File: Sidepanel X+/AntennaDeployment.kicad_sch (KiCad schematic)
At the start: 5 parts, among them Q1 BSS214NW

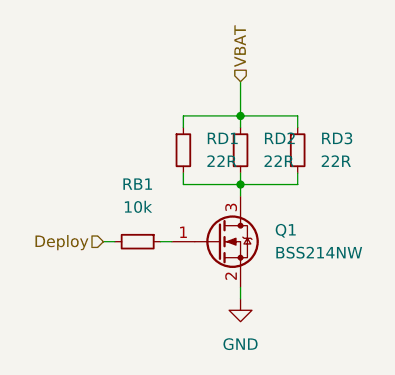
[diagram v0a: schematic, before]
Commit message: Changed the layout of all the sidepanel PCBs to mitigate the problems that arised from the bad previous design.
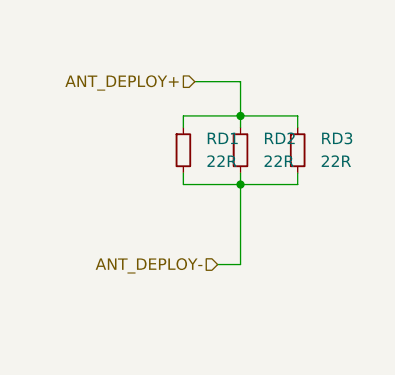
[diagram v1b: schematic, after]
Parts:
- removed Q1: BSS214NW, Package_TO_SOT_SMD:SOT-323_SC-70, symbol Transistor_FET:BSS214NW
- removed RB1: 10k, Resistor_SMD:R_0603_1608Metric, symbol Device:R_Small
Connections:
- net ANT_DEPLOY-: now reaches RD1.2, RD2.2, RD3.2
- net VBAT renamed ANT_DEPLOY+
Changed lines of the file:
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@@
-(kicad_sch (version 20211123) (generator eeschema)
+(kicad_sch (version 20230121) (generator eeschema)
   (paper "A4")
   (junction (at 35.56 39.37) (diameter 0) (color 0 0 0 0)
@@
   )
   (wire (pts (xy 29.21 33.02) (xy 29.21 31.75))
-    (stroke (width 0) (type default) (color 0 0 0 0))
+    (stroke (width 0) (type default))
   )
   (wire (pts (xy 29.21 39.37) (xy 35.56 39.37))
-    (stroke (width 0) (type default) (color 0 0 0 0))
+    (stroke (width 0) (type default))
   )
-  (wire (pts (xy 26.67 45.72) (xy 27.94 45.72))
-    (stroke (width 0) (type default) (color 0 0 0 0))
-  )
-  (wire (pts (xy 35.56 39.37) (xy 35.56 40.64))
-    (stroke (width 0) (type default) (color 0 0 0 0))
-  )
-  (wire (pts (xy 35.56 50.8) (xy 35.56 52.07))
-    (stroke (width 0) (type default) (color 0 0 0 0))
+  (wire (pts (xy 35.56 39.37) (xy 35.56 48.26))
+    (stroke (width 0) (type default))
   )
   (wire (pts (xy 35.56 31.75) (xy 35.56 33.02))
-    (stroke (width 0) (type default) (color 0 0 0 0))
+    (stroke (width 0) (type default))
+  )
+  (wire (pts (xy 30.48 27.94) (xy 35.56 27.94))
+    (stroke (width 0) (type default))
   )
   (wire (pts (xy 35.56 39.37) (xy 41.91 39.37))
-    (stroke (width 0) (type default) (color 0 0 0 0))
+    (stroke (width 0) (type default))
   )
   (wire (pts (xy 29.21 38.1) (xy 29.21 39.37))
-    (stroke (width 0) (type default) (color 0 0 0 0))
-  )
-  (wire (pts (xy 20.32 45.72) (xy 21.59 45.72))
-    (stroke (width 0) (type default) (color 0 0 0 0))
+    (stroke (width 0) (type default))
   )
   (wire (pts (xy 35.56 38.1) (xy 35.56 39.37))
-    (stroke (width 0) (type default) (color 0 0 0 0))
+    (stroke (width 0) (type default))
   )
   (wire (pts (xy 29.21 31.75) (xy 35.56 31.75))
-    (stroke (width 0) (type default) (color 0 0 0 0))
+    (stroke (width 0) (type default))
   )
   (wire (pts (xy 41.91 31.75) (xy 41.91 33.02))
-    (stroke (width 0) (type default) (color 0 0 0 0))
+    (stroke (width 0) (type default))
+  )
+  (wire (pts (xy 35.56 48.26) (xy 33.02 48.26))
+    (stroke (width 0) (type default))
   )
   (wire (pts (xy 41.91 39.37) (xy 41.91 38.1))
-    (stroke (width 0) (type default) (color 0 0 0 0))
+    (stroke (width 0) (type default))
   )
   (wire (pts (xy 35.56 27.94) (xy 35.56 31.75))
-    (stroke (width 0) (type default) (color 0 0 0 0))
+    (stroke (width 0) (type default))
   )
   (wire (pts (xy 35.56 31.75) (xy 41.91 31.75))
-    (stroke (width 0) (type default) (color 0 0 0 0))
+    (stroke (width 0) (type default))
   )
-  (hierarchical_label "VBAT" (shape input) (at 35.56 27.94 90)
-    (effects (font (size 1.27 1.27)) (justify left))
+  (hierarchical_label "ANT_DEPLOY-" (shape input) (at 33.02 48.26 180) (fields_autoplaced)
+    (effects (font (size 1.27 1.27)) (justify right))
   )
-  (hierarchical_label "Deploy" (shape input) (at 20.32 45.72 180)
+  (hierarchical_label "ANT_DEPLOY+" (shape input) (at 30.48 27.94 180) (fields_autoplaced)
     (effects (font (size 1.27 1.27)) (justify right))
   )
   (symbol (lib_id "Device:R_Small") (at 35.56 35.56 0) (unit 1)
-    (in_bom yes) (on_board yes) (fields_autoplaced)
-    (property "Reference" "RD2" (id 0) (at 38.1 34.2899 0)
+    (in_bom yes) (on_board yes) (dnp no) (fields_autoplaced)
+    (property "Reference" "RD2" (at 38.1 34.2899 0)
       (effects (font (size 1.27 1.27)) (justify left))
     )
-    (property "Value" "22R" (id 1) (at 38.1 36.8299 0)
+    (property "Value" "22R" (at 38.1 36.8299 0)
       (effects (font (size 1.27 1.27)) (justify left))
     )
-    (property "Footprint" "Resistor_SMD:R_MiniMELF_MMA-0204" (id 2) (at 35.56 35.56 0)
+    (property "Footprint" "Resistor_SMD:R_MiniMELF_MMA-0204" (at 35.56 35.56 0)
       (effects (font (size 1.27 1.27)) hide)
     )
-    (property "Datasheet" "~" (id 3) (at 35.56 35.56 0)
+    (property "Datasheet" "~" (at 35.56 35.56 0)
       (effects (font (size 1.27 1.27)) hide)
     )
     (pin "1")
     (pin "2")
+    (instances
+      (project "STS1_SIDEPANEL"
+        (path "/e63e39d7-6ac0-4ffd-8aa3-1841a4541b55/13fd01c2-9c13-4b4c-bd8b-0bea989ca11e"
+          (reference "RD2") (unit 1)
+        )
+      )
+    )
   )
-  (symbol (lib_id "Device:R_Small") (at 24.13 45.72 270) (unit 1)
-    (in_bom yes) (on_board yes) (fields_autoplaced)
-    (property "Reference" "RB1" (id 0) (at 24.13 39.37 90))
-    (property "Value" "10k" (id 1) (at 24.13 41.91 90))
-    (property "Footprint" "Resistor_SMD:R_0603_1608Metric" (id 2) (at 24.13 45.72 0)
+  (symbol (lib_id "Device:R_Small") (at 41.91 35.56 0) (unit 1)
+    (in_bom yes) (on_board yes) (dnp no) (fields_autoplaced)
+    (property "Reference" "RD3" (at 44.45 34.2899 0)
+      (effects (font (size 1.27 1.27)) (justify left))
+    )
+    (property "Value" "22R" (at 44.45 36.8299 0)
+      (effects (font (size 1.27 1.27)) (justify left))
+    )
+    (property "Footprint" "Resistor_SMD:R_MiniMELF_MMA-0204" (at 41.91 35.56 0)
       (effects (font (size 1.27 1.27)) hide)
     )
-    (property "Datasheet" "~" (id 3) (at 24.13 45.72 0)
+    (property "Datasheet" "~" (at 41.91 35.56 0)
       (effects (font (size 1.27 1.27)) hide)
     )
     (pin "1")
     (pin "2")
+    (instances
+      (project "STS1_SIDEPANEL"
+        (path "/e63e39d7-6ac0-4ffd-8aa3-1841a4541b55/13fd01c2-9c13-4b4c-bd8b-0bea989ca11e"
+          (reference "RD3") (unit 1)
+        )
+      )
+    )
   )
-  (symbol (lib_id "Transistor_FET:BSS214NW") (at 33.02 45.72 0) (unit 1)
-    (in_bom yes) (on_board yes) (fields_autoplaced)
-    (property "Reference" "Q1" (id 0) (at 39.37 44.4499 0)
+  (symbol (lib_id "Device:R_Small") (at 29.21 35.56 0) (unit 1)
+    (in_bom yes) (on_board yes) (dnp no) (fields_autoplaced)
+    (property "Reference" "RD1" (at 31.75 34.2899 0)
       (effects (font (size 1.27 1.27)) (justify left))
     )
-    (property "Value" "BSS214NW" (id 1) (at 39.37 46.9899 0)
+    (property "Value" "22R" (at 31.75 36.8299 0)
       (effects (font (size 1.27 1.27)) (justify left))
     )
-    (property "Footprint" "Package_TO_SOT_SMD:SOT-323_SC-70" (id 2) (at 38.1 47.625 0)
-      (effects (font (size 1.27 1.27) italic) (justify left) hide)
-    )
-    (property "Datasheet" "https://www.infineon.com/dgdl/Infineon-BSS214NW-DS-v02_02-en.pdf?fileId=db3a30431b3e89eb011b695aebc01bde" (id 3) (at 33.02 45.72 0)
-      (effects (font (size 1.27 1.27)) (justify left) hide)
-    )
-    (pin "1")
-    (pin "2")
-    (pin "3")
-  )
-  (symbol (lib_id "Device:R_Small") (at 41.91 35.56 0) (unit 1)
-    (in_bom yes) (on_board yes) (fields_autoplaced)
-    (property "Reference" "RD3" (id 0) (at 44.45 34.2899 0)
-      (effects (font (size 1.27 1.27)) (justify left))
-    )
-    (property "Value" "22R" (id 1) (at 44.45 36.8299 0)
-      (effects (font (size 1.27 1.27)) (justify left))
-    )
-    (property "Footprint" "Resistor_SMD:R_MiniMELF_MMA-0204" (id 2) (at 41.91 35.56 0)
+    (property "Footprint" "Resistor_SMD:R_MiniMELF_MMA-0204" (at 29.21 35.56 0)
       (effects (font (size 1.27 1.27)) hide)
     )
-    (property "Datasheet" "~" (id 3) (at 41.91 35.56 0)
+    (property "Datasheet" "~" (at 29.21 35.56 0)
       (effects (font (size 1.27 1.27)) hide)
     )
     (pin "1")
     (pin "2")
-  )
-  (symbol (lib_id "Device:R_Small") (at 29.21 35.56 0) (unit 1)
-    (in_bom yes) (on_board yes) (fields_autoplaced)
-    (property "Reference" "RD1" (id 0) (at 31.75 34.2899 0)
-      (effects (font (size 1.27 1.27)) (justify left))
+    (instances
+      (project "STS1_SIDEPANEL"
+        (path "/e63e39d7-6ac0-4ffd-8aa3-1841a4541b55/13fd01c2-9c13-4b4c-bd8b-0bea989ca11e"
+          (reference "RD1") (unit 1)
+        )
+      )
     )
-    (property "Value" "22R" (id 1) (at 31.75 36.8299 0)
-      (effects (font (size 1.27 1.27)) (justify left))
-    )
-    (property "Footprint" "Resistor_SMD:R_MiniMELF_MMA-0204" (id 2) (at 29.21 35.56 0)
-      (effects (font (size 1.27 1.27)) hide)
-    )
-    (property "Datasheet" "~" (id 3) (at 29.21 35.56 0)
-      (effects (font (size 1.27 1.27)) hide)
-    )
-    (pin "1")
-    (pin "2")
-  )
-  (symbol (lib_id "power:GND") (at 35.56 52.07 0) (unit 1)
-    (in_bom yes) (on_board yes) (fields_autoplaced)
-    (property "Reference" "#PWR05" (id 0) (at 35.56 58.42 0)
-      (effects (font (size 1.27 1.27)) hide)
-    )
-    (property "Value" "GND" (id 1) (at 35.56 57.15 0))
-    (property "Footprint" "" (id 2) (at 35.56 52.07 0)
-      (effects (font (size 1.27 1.27)) hide)
-    )
-    (property "Datasheet" "" (id 3) (at 35.56 52.07 0)
-      (effects (font (size 1.27 1.27)) hide)
-    )
-    (pin "1")
   )
 )
